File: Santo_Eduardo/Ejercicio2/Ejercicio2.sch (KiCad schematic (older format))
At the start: 0 parts

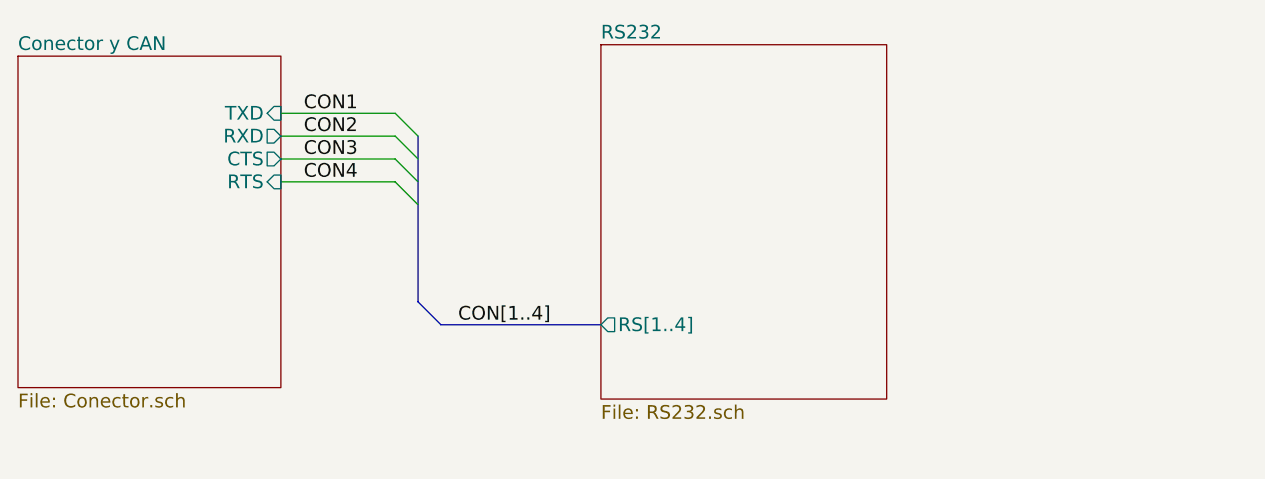
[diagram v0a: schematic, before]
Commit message: Added GND planes
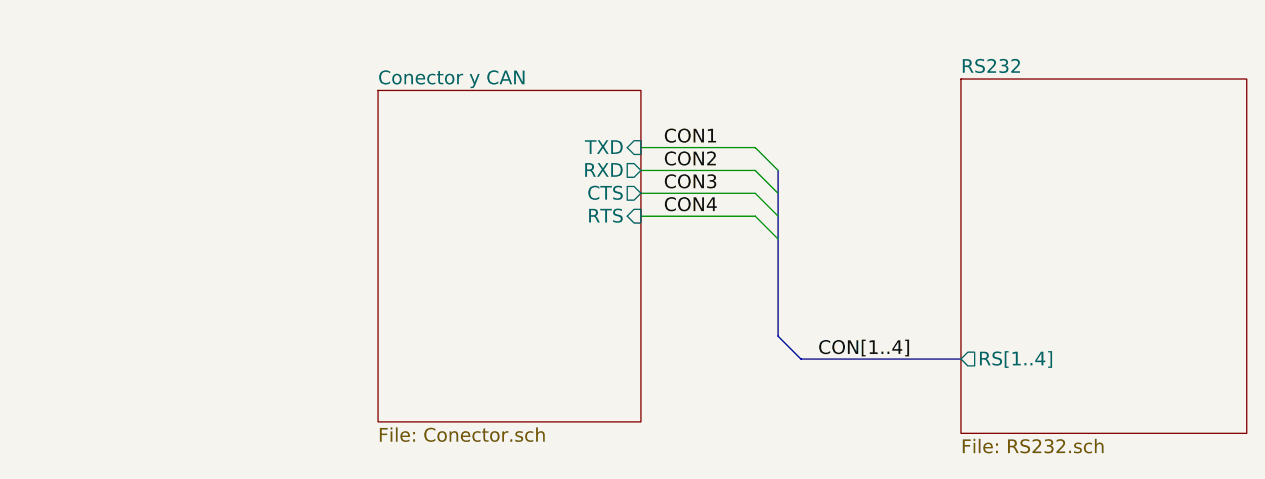
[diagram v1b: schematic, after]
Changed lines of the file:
@@
 $EndDescr
 $Sheet
-S 2500 2550 1150 1450
+S 4075 2700 1150 1450
 U 565DDB6F
 F0 "Conector y CAN" 60
 F1 "Conector.sch" 60
-F2 "TXD" I R 3650 2800 60
-F3 "RXD" O R 3650 2900 60
-F4 "CTS" O R 3650 3000 60
-F5 "RTS" I R 3650 3100 60
+F2 "TXD" I R 5225 2950 60
+F3 "RXD" O R 5225 3050 60
+F4 "CTS" O R 5225 3150 60
+F5 "RTS" I R 5225 3250 60
 $EndSheet
 $Sheet
-S 5050 2500 1250 1550
+S 6625 2650 1250 1550
 U 565DDB8C
 F0 "RS232" 60
 F1 "RS232.sch" 60
-F2 "RS[1..4]" O L 5050 3725 60
+F2 "RS[1..4]" O L 6625 3875 60
 $EndSheet
 Entry Bus Bus
-	4250 3625 4350 3725
+	5825 3775 5925 3875
 Wire Bus Line
-	4350 3725 5050 3725
+	5925 3875 6625 3875
 Entry Wire Line
-	4150 2800 4250 2900
+	5725 2950 5825 3050
 Entry Wire Line
-	4150 2900 4250 3000
+	5725 3050 5825 3150
 Entry Wire Line
-	4150 3000 4250 3100
+	5725 3150 5825 3250
 Entry Wire Line
-	4150 3100 4250 3200
+	5725 3250 5825 3350
 Wire Bus Line
-	4250 3625 4250 2900
+	5825 3775 5825 3050
 Wire Wire Line
-	3650 2800 4150 2800
+	5225 2950 5725 2950
 Wire Wire Line
-	3650 2900 4150 2900
+	5225 3050 5725 3050
 Wire Wire Line
-	3650 3000 4150 3000
+	5225 3150 5725 3150
 Wire Wire Line
-	3650 3100 4150 3100
-Text Label 3750 2800 0    60   ~ 0
+	5225 3250 5725 3250
+Text Label 5325 2950 0    60   ~ 0
 CON1
-Text Label 3750 2900 0    60   ~ 0
+Text Label 5325 3050 0    60   ~ 0
 CON2
-Text Label 3750 3000 0    60   ~ 0
+Text Label 5325 3150 0    60   ~ 0
 CON3
-Text Label 3750 3100 0    60   ~ 0
+Text Label 5325 3250 0    60   ~ 0
 CON4
-Text Label 4425 3725 0    60   ~ 0
+Text Label 6000 3875 0    60   ~ 0
 CON[1..4]
 $EndSCHEMATC
